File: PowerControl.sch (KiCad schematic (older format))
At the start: 22 parts, among them J1 Conn_01x02, J2 Emergency_stop_switch, J3 Emergency_stop_switch, J4 XT60PB-F, J5 XT60PB-M, Q1 Q_PMOS_GDS, Q2 Q_PMOS_GDS, U1 TLP621, U2 TLV76012DBZR

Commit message: Add board
基本的な設計が終了
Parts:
- added H1, H2, H3, H4: MountingHole, MountingHole:MountingHole_3.2mm_M3, symbol Mechanical:MountingHole
- C1: footprint (none) -> Capacitor_THT:CP_Radial_D12.5mm_P5.00mm
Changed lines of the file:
@@
 Wire Wire Line
 	8050 3900 8050 3950
-$Comp
-L power:VCC #PWR09
-U 1 1 5EF2872A
-P 6400 4950
-F 0 "#PWR09" H 6400 4800 50  0001 C CNN
-F 1 "VCC" H 6415 5123 50  0000 C CNN
-F 2 "" H 6400 4950 50  0001 C CNN
-F 3 "" H 6400 4950 50  0001 C CNN
-	1    6400 4950
-	1    0    0    -1
-$EndComp
 Text GLabel 8150 3800 0    50   Input ~ 0
 OutPut
@@
 Wire Wire Line
 	6400 5050 6400 5200
-Wire Wire Line
-	6400 4950 6400 5050
 Connection ~ 6400 5050
 $Comp
@@
 F 0 "C1" H 1868 3496 50  0000 L CNN
 F 1 "1000u" H 1868 3405 50  0000 L CNN
-F 2 "" H 1788 3300 50  0001 C CNN
+F 2 "Capacitor_THT:CP_Radial_D12.5mm_P5.00mm" H 1788 3300 50  0001 C CNN
 F 3 "~" H 1750 3450 50  0001 C CNN
 	1    1750 3450
@@
 Wire Wire Line
 	5250 5400 5700 5400
+Wire Wire Line
+	6400 4950 6400 5050
+$Comp
+L power:VCC #PWR09
+U 1 1 5EF2872A
+P 6400 4950
+F 0 "#PWR09" H 6400 4800 50  0001 C CNN
+F 1 "VCC" H 6415 5123 50  0000 C CNN
+F 2 "" H 6400 4950 50  0001 C CNN
+F 3 "" H 6400 4950 50  0001 C CNN
+	1    6400 4950
+	1    0    0    -1
+$EndComp
+$Comp
+L Mechanical:MountingHole H1
+U 1 1 5EF2F027
+P 5550 3450
+F 0 "H1" H 5650 3496 50  0000 L CNN
+F 1 "MountingHole" H 5650 3405 50  0000 L CNN
+F 2 "MountingHole:MountingHole_3.2mm_M3" H 5550 3450 50  0001 C CNN
+F 3 "~" H 5550 3450 50  0001 C CNN
+	1    5550 3450
+	1    0    0    -1
+$EndComp
+$Comp
+L Mechanical:MountingHole H3
+U 1 1 5EF2FEEF
+P 6250 3450
+F 0 "H3" H 6350 3496 50  0000 L CNN
+F 1 "MountingHole" H 6350 3405 50  0000 L CNN
+F 2 "MountingHole:MountingHole_3.2mm_M3" H 6250 3450 50  0001 C CNN
+F 3 "~" H 6250 3450 50  0001 C CNN
+	1    6250 3450
+	1    0    0    -1
+$EndComp
+$Comp
+L Mechanical:MountingHole H2
+U 1 1 5EF30E40
+P 5550 3650
+F 0 "H2" H 5650 3696 50  0000 L CNN
+F 1 "MountingHole" H 5650 3605 50  0000 L CNN
+F 2 "MountingHole:MountingHole_3.2mm_M3" H 5550 3650 50  0001 C CNN
+F 3 "~" H 5550 3650 50  0001 C CNN
+	1    5550 3650
+	1    0    0    -1
+$EndComp
+$Comp
+L Mechanical:MountingHole H4
+U 1 1 5EF31C67
+P 6250 3650
+F 0 "H4" H 6350 3696 50  0000 L CNN
+F 1 "MountingHole" H 6350 3605 50  0000 L CNN
+F 2 "MountingHole:MountingHole_3.2mm_M3" H 6250 3650 50  0001 C CNN
+F 3 "~" H 6250 3650 50  0001 C CNN
+	1    6250 3650
+	1    0    0    -1
+$EndComp
 $EndSCHEMATC

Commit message: change Pch MOSFET name
Pch MOSFETの名称をIPD80P03P4L-07に変更
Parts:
- Q1, Q2: value Q_PMOS_GDS -> IPD80P03P4L-07
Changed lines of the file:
@@
 U 1 1 5EF097AB
 P 6300 5400
-F 0 "Q1" H 6505 5354 50  0000 L CNN
-F 1 "Q_PMOS_GDS" H 6505 5445 50  0000 L CNN
+F 0 "Q1" H 6504 5354 50  0000 L CNN
+F 1 "IPD80P03P4L-07" H 6504 5445 50  0000 L CNN
 F 2 "Package_TO_SOT_SMD:TO-252-2" H 6500 5500 50  0001 C CNN
 F 3 "~" H 6300 5400 50  0001 C CNN
@@
 U 1 1 5EF2BF51
 P 7300 5400
-F 0 "Q2" H 7505 5354 50  0000 L CNN
-F 1 "Q_PMOS_GDS" H 7505 5445 50  0000 L CNN
+F 0 "Q2" H 7504 5354 50  0000 L CNN
+F 1 "IPD80P03P4L-07" H 7504 5445 50  0000 L CNN
 F 2 "Package_TO_SOT_SMD:TO-252-2" H 7500 5500 50  0001 C CNN
 F 3 "~" H 7300 5400 50  0001 C CNN

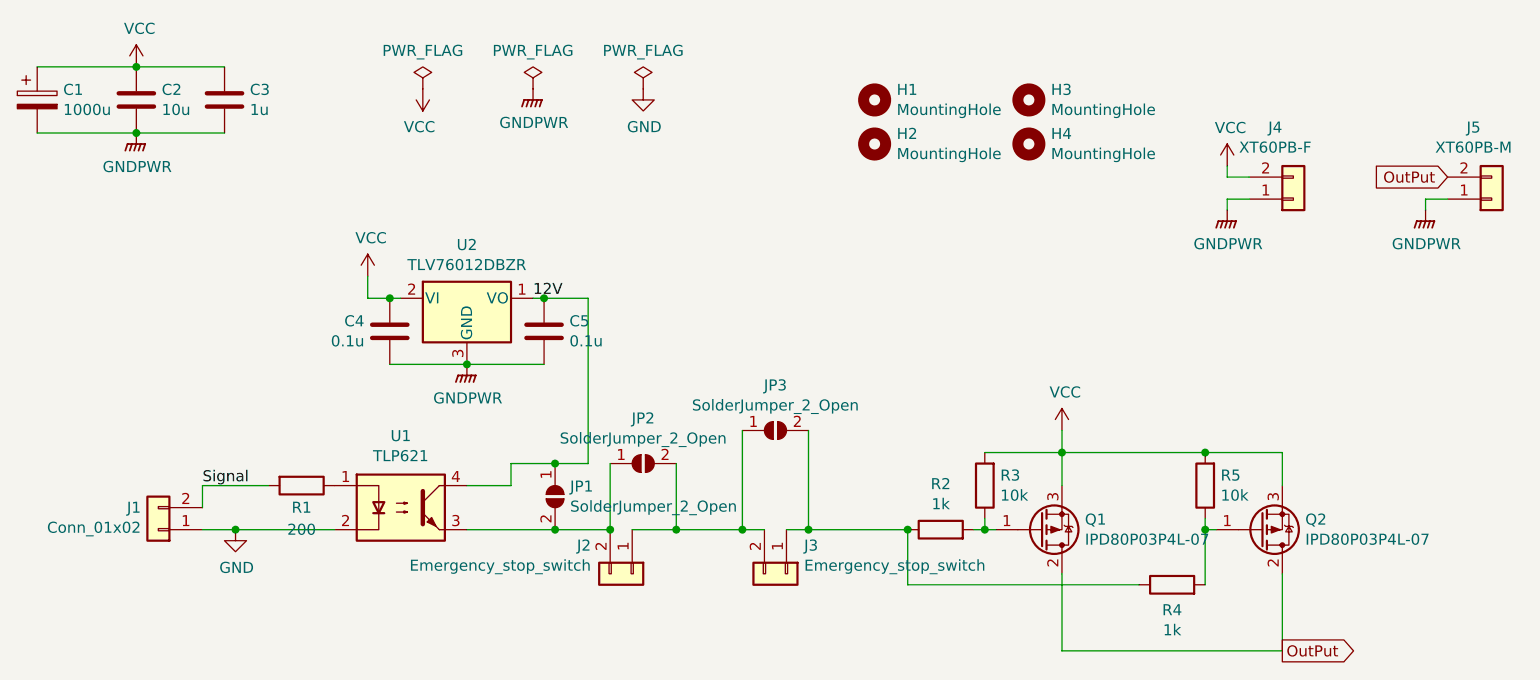
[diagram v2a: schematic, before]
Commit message: Fix: Pch MOSFETのゲートの印加電圧を修正(12V→GND)
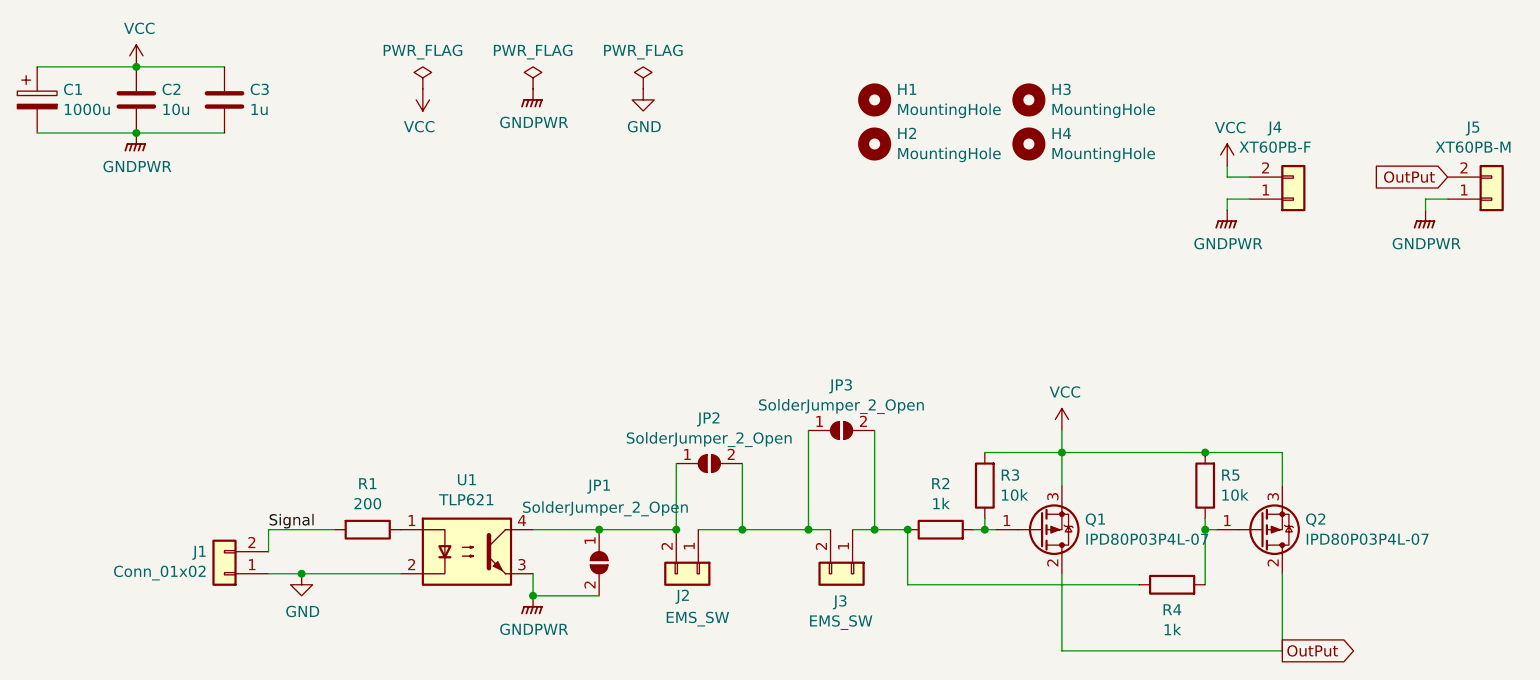
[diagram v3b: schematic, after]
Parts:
- removed C4, C5: 0.1u, Capacitor_SMD:C_0805_2012Metric_Pad1.15x1.40mm_HandSolder, symbol Device:C
- removed U2: TLV76012DBZR, Package_TO_SOT_SMD:TSOT-23_HandSoldering, symbol Regulator_Linear:LM3480-12
- J2, J3: value Emergency_stop_switch -> EMS_SW
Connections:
- net 12V is gone; now on an unnamed net: JP1.1 (A), U1.4
- net GNDPWR: now also JP1.2 (B), U1.3
- net at J2.2 (Pin_2), JP2.1 (A): no longer JP1.2 (B), U1.3
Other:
- moved on the sheet: J1, J2, J3, JP1, JP2, JP3, R1, U1
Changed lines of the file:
@@
-	1    0    0    -1
-$EndComp
-Text Label 2500 5200 0    50   ~ 0
-Signal
-Wire Wire Line
-	2500 5300 2500 5200
-Wire Wire Line
-	2650 5400 2500 5400
-$Comp
-L power:GND #PWR03
-U 1 1 5EF1071A
-P 2650 5400
-F 0 "#PWR03" H 2650 5150 50  0001 C CNN
-F 1 "GND" H 2655 5227 50  0000 C CNN
-F 2 "" H 2650 5400 50  0001 C CNN
-F 3 "" H 2650 5400 50  0001 C CNN
-	1    2650 5400
-	1    0    0    -1
-$EndComp
-$Comp
-L Connector_Generic:Conn_01x02 J1
-U 1 1 5EF109E6
-P 2300 5400
-F 0 "J1" H 2379 5300 50  0000 L CNN
-F 1 "Conn_01x02" H 2379 5391 50  0000 L CNN
-F 2 "Connector_PinHeader_2.54mm:PinHeader_1x02_P2.54mm_Vertical" H 2300 5400 50  0001 C CNN
-F 3 "~" H 2300 5400 50  0001 C CNN
-	1    2300 5400
-	-1   0    0    1
-$EndComp
-$Comp
-L Isolator:PC817 U1
-U 1 1 5EF0F04E
-P 3400 5300
-F 0 "U1" H 3400 5625 50  0000 C CNN
-F 1 "TLP621" H 3400 5534 50  0000 C CNN
-F 2 "Package_DIP:DIP-4_W7.62mm" H 3200 5100 50  0001 L CIN
-F 3 "http://www.soselectronic.cz/a_info/resource/d/pc817.pdf" H 3400 5300 50  0001 L CNN
-	1    3400 5300
 	1    0    0    -1
 $EndComp
@@
 Connection ~ 6400 5050
 $Comp
-L Device:R R1
-U 1 1 5EF32C60
-P 2950 5200
-F 0 "R1" V 3050 5200 50  0000 C CNN
-F 1 "200" V 3150 5200 50  0000 C CNN
-F 2 "Resistor_SMD:R_0603_1608Metric_Pad1.05x0.95mm_HandSolder" V 2880 5200 50  0001 C CNN
-F 3 "~" H 2950 5200 50  0001 C CNN
-	1    2950 5200
-	0    1    1    0
-$EndComp
-Connection ~ 2650 5400
-Wire Wire Line
-	2650 5400 3100 5400
-Wire Wire Line
-	2500 5200 2800 5200
-$Comp
-L Connector_Generic:Conn_01x02 J2
-U 1 1 5EF40D5E
-P 4450 5600
-F 0 "J2" V 4322 5413 50  0000 R CNN
-F 1 "Emergency_stop_switch" V 4413 5413 50  0000 R CNN
-F 2 "Connector_PinHeader_2.54mm:PinHeader_1x02_P2.54mm_Vertical" H 4450 5600 50  0001 C CNN
-F 3 "~" H 4450 5600 50  0001 C CNN
-	1    4450 5600
-	0    1    1    0
-$EndComp
-$Comp
-L Connector_Generic:Conn_01x02 J3
-U 1 1 5EF41305
-P 5150 5600
-F 0 "J3" V 5022 5680 50  0000 L CNN
-F 1 "Emergency_stop_switch" V 5113 5680 50  0000 L CNN
-F 2 "Connector_PinHeader_2.54mm:PinHeader_1x02_P2.54mm_Vertical" H 5150 5600 50  0001 C CNN
-F 3 "~" H 5150 5600 50  0001 C CNN
-	1    5150 5600
-	0    1    1    0
-$EndComp
-Wire Wire Line
-	3250 4250 3250 4350
-$Comp
-L power:VCC #PWR04
-U 1 1 5EF16864
-P 3250 4250
-F 0 "#PWR04" H 3250 4100 50  0001 C CNN
-F 1 "VCC" H 3265 4423 50  0000 C CNN
-F 2 "" H 3250 4250 50  0001 C CNN
-F 3 "" H 3250 4250 50  0001 C CNN
-	1    3250 4250
-	1    0    0    -1
-$EndComp
-$Comp
-L Regulator_Linear:LM3480-12 U2
-U 1 1 5EF1540F
-P 3700 4350
-F 0 "U2" H 3700 4592 50  0000 C CNN
-F 1 "TLV76012DBZR" H 3700 4501 50  0000 C CNN
-F 2 "Package_TO_SOT_SMD:TSOT-23_HandSoldering" H 3725 4200 50  0001 L CIN
-F 3 "" H 3700 4300 50  0001 C CNN
-	1    3700 4350
-	1    0    0    -1
-$EndComp
-Wire Wire Line
-	4250 4350 4250 5100
-$Comp
 L Connector_Generic:Conn_01x02 J4
 U 1 1 5EF2467C
@@
 	1    0    0    1
 $EndComp
-Wire Wire Line
-	4000 4350 4050 4350
-$Comp
-L power:GNDPWR #PWR06
-U 1 1 5EF1CE2F
-P 3700 4650
-F 0 "#PWR06" H 3700 4450 50  0001 C CNN
-F 1 "GNDPWR" H 3704 4496 50  0000 C CNN
-F 2 "" H 3700 4600 50  0001 C CNN
-F 3 "" H 3700 4600 50  0001 C CNN
-	1    3700 4650
-	1    0    0    -1
-$EndComp
-Text Label 4000 4350 0    50   ~ 0
-12V
 $Comp
 L Device:Q_PMOS_GDS Q2
@@
 $EndComp
 $Comp
-L Device:C C5
-U 1 1 5EF510BF
-P 4050 4500
-F 0 "C5" H 4165 4546 50  0000 L CNN
-F 1 "0.1u" H 4165 4455 50  0000 L CNN
-F 2 "Capacitor_SMD:C_0805_2012Metric_Pad1.15x1.40mm_HandSolder" H 4088 4350 50  0001 C CNN
-F 3 "~" H 4050 4500 50  0001 C CNN
-	1    4050 4500
-	1    0    0    -1
-$EndComp
-$Comp
-L Device:C C4
-U 1 1 5EF519D9
-P 3350 4500
-F 0 "C4" H 3235 4546 50  0000 R CNN
-F 1 "0.1u" H 3235 4455 50  0000 R CNN
-F 2 "Capacitor_SMD:C_0805_2012Metric_Pad1.15x1.40mm_HandSolder" H 3388 4350 50  0001 C CNN
-F 3 "~" H 3350 4500 50  0001 C CNN
-	1    3350 4500
-	1    0    0    -1
-$EndComp
-Connection ~ 4050 4350
-Wire Wire Line
-	3700 5200 3900 5200
-Wire Wire Line
-	3250 4350 3350 4350
-Connection ~ 3350 4350
-Wire Wire Line
-	3350 4350 3400 4350
-Wire Wire Line
-	4050 4650 3700 4650
-Connection ~ 3700 4650
-Wire Wire Line
-	3700 4650 3350 4650
-Wire Wire Line
-	4050 4350 4250 4350
-$Comp
 L Device:CP C1
 U 1 1 5EF5DFD2
@@
 $EndComp
 Wire Wire Line
-	3900 5100 3900 5200
-Connection ~ 4100 5100
-Wire Wire Line
-	4100 5100 3900 5100
-Wire Wire Line
-	4100 5100 4250 5100
-Wire Wire Line
-	3700 5400 4100 5400
-Connection ~ 4100 5400
-Wire Wire Line
-	4100 5400 4350 5400
-$Comp
-L Jumper:SolderJumper_2_Open JP3
-U 1 1 5EF13331
-P 5100 4950
-F 0 "JP3" H 5100 5155 50  0000 C CNN
-F 1 "SolderJumper_2_Open" H 5100 5064 50  0000 C CNN
-F 2 "Jumper:SolderJumper-2_P1.3mm_Open_TrianglePad1.0x1.5mm" H 5100 4950 50  0001 C CNN
-F 3 "~" H 5100 4950 50  0001 C CNN
-	1    5100 4950
-	1    0    0    -1
-$EndComp
-$Comp
-L Jumper:SolderJumper_2_Open JP2
-U 1 1 5EF3F971
-P 4500 5100
-F 0 "JP2" H 4500 5305 50  0000 C CNN
-F 1 "SolderJumper_2_Open" H 4500 5214 50  0000 C CNN
-F 2 "Jumper:SolderJumper-2_P1.3mm_Open_TrianglePad1.0x1.5mm" H 4500 5100 50  0001 C CNN
-F 3 "~" H 4500 5100 50  0001 C CNN
-	1    4500 5100
-	1    0    0    -1
-$EndComp
-$Comp
-L Jumper:SolderJumper_2_Open JP1
-U 1 1 5EF1E5F2
-P 4100 5250
-F 0 "JP1" V 4054 5318 50  0000 L CNN
-F 1 "SolderJumper_2_Open" V 4145 5318 50  0000 L CNN
-F 2 "Jumper:SolderJumper-2_P1.3mm_Open_TrianglePad1.0x1.5mm" H 4100 5250 50  0001 C CNN
-F 3 "~" H 4100 5250 50  0001 C CNN
-	1    4100 5250
-	0    1    1    0
-$EndComp
-Wire Wire Line
-	5150 5400 5250 5400
-Wire Wire Line
-	4450 5400 4650 5400
-Wire Wire Line
-	4350 5100 4350 5400
-Connection ~ 4350 5400
-Wire Wire Line
-	4650 5100 4650 5400
-Connection ~ 4650 5400
-Wire Wire Line
-	4650 5400 4950 5400
-Wire Wire Line
-	4950 4950 4950 5400
-Connection ~ 4950 5400
-Wire Wire Line
-	4950 5400 5050 5400
+	5450 5400 5550 5400
 Wire Wire Line
 	5250 4950 5250 5400
 Connection ~ 5250 5400
 Wire Wire Line
-	5250 5400 5700 5400
+	5250 5400 5350 5400
+Wire Wire Line
+	5550 4950 5550 5400
+Connection ~ 5550 5400
+Wire Wire Line
+	5550 5400 5700 5400
 Wire Wire Line
 	6400 4950 6400 5050
@@
 	1    0    0    -1
 $EndComp
+$Comp
+L Connector_Generic:Conn_01x02 J3
+U 1 1 5EF41305
+P 5450 5600
+F 0 "J3" V 5575 5546 50  0000 C CNN
+F 1 "EMS_SW" V 5666 5546 50  0000 C CNN
+F 2 "Connector_PinHeader_2.54mm:PinHeader_1x02_P2.54mm_Vertical" H 5450 5600 50  0001 C CNN
+F 3 "~" H 5450 5600 50  0001 C CNN
+	1    5450 5600
+	0    1    1    0
+$EndComp
+Text Label 2800 5400 0    50   ~ 0
+Signal
+Wire Wire Line
+	2800 5500 2800 5400
+Wire Wire Line
+	2950 5600 2800 5600
+$Comp
+L power:GND #PWR03
+U 1 1 5EF1071A
+P 2950 5600
+F 0 "#PWR03" H 2950 5350 50  0001 C CNN
+F 1 "GND" H 2955 5427 50  0000 C CNN
+F 2 "" H 2950 5600 50  0001 C CNN
+F 3 "" H 2950 5600 50  0001 C CNN
+	1    2950 5600
+	1    0    0    -1
+$EndComp
+$Comp
+L Connector_Generic:Conn_01x02 J1
+U 1 1 5EF109E6
+P 2600 5600
+F 0 "J1" H 2679 5500 50  0000 L CNN
+F 1 "Conn_01x02" H 2679 5591 50  0000 L CNN
+F 2 "Connector_PinHeader_2.54mm:PinHeader_1x02_P2.54mm_Vertical" H 2600 5600 50  0001 C CNN
+F 3 "~" H 2600 5600 50  0001 C CNN
+	1    2600 5600
+	-1   0    0    1
+$EndComp
+$Comp
+L Device:R R1
+U 1 1 5EF32C60
+P 3250 5400
+F 0 "R1" V 3043 5400 50  0000 C CNN
+F 1 "200" V 3134 5400 50  0000 C CNN
+F 2 "Resistor_SMD:R_0603_1608Metric_Pad1.05x0.95mm_HandSolder" V 3180 5400 50  0001 C CNN
+F 3 "~" H 3250 5400 50  0001 C CNN
+	1    3250 5400
+	0    1    1    0
+$EndComp
+Connection ~ 2950 5600
+Wire Wire Line
+	2950 5600 3400 5600
+Wire Wire Line
+	2800 5400 3100 5400
+$Comp
+L Connector_Generic:Conn_01x02 J2
+U 1 1 5EF40D5E
+P 4750 5600
+F 0 "J2" V 4850 5500 50  0000 L CNN
+F 1 "EMS_SW" V 4950 5450 50  0000 L CNN
+F 2 "Connector_PinHeader_2.54mm:PinHeader_1x02_P2.54mm_Vertical" H 4750 5600 50  0001 C CNN
+F 3 "~" H 4750 5600 50  0001 C CNN
+	1    4750 5600
+	0    1    1    0
+$EndComp
+$Comp
+L Jumper:SolderJumper_2_Open JP1
+U 1 1 5EF1E5F2
+P 4300 5550
+F 0 "JP1" V 3950 5500 50  0000 L CNN
+F 1 "SolderJumper_2_Open" V 4050 5200 50  0000 L CNN
+F 2 "Jumper:SolderJumper-2_P1.3mm_Open_TrianglePad1.0x1.5mm" H 4300 5550 50  0001 C CNN
+F 3 "~" H 4300 5550 50  0001 C CNN
+	1    4300 5550
+	0    1    1    0
+$EndComp
+Wire Wire Line
+	4750 5400 4950 5400
+Wire Wire Line
+	4650 5100 4650 5400
+Connection ~ 4650 5400
+$Comp
+L Isolator:PC817 U1
+U 1 1 5EF0F04E
+P 3700 5500
+F 0 "U1" H 3700 5825 50  0000 C CNN
+F 1 "TLP621" H 3700 5734 50  0000 C CNN
+F 2 "Package_DIP:DIP-4_W7.62mm" H 3500 5300 50  0001 L CIN
+F 3 "http://www.soselectronic.cz/a_info/resource/d/pc817.pdf" H 3700 5500 50  0001 L CNN
+	1    3700 5500
+	1    0    0    -1
+$EndComp
+Wire Wire Line
+	4000 5400 4300 5400
+$Comp
+L power:GNDPWR #PWR?
+U 1 1 61447DCE
+P 4000 5700
+F 0 "#PWR?" H 4000 5500 50  0001 C CNN
+F 1 "GNDPWR" H 4004 5546 50  0000 C CNN
+F 2 "" H 4000 5650 50  0001 C CNN
+F 3 "" H 4000 5650 50  0001 C CNN
+	1    4000 5700
+	1    0    0    -1
+$EndComp
+Connection ~ 4300 5400
+Wire Wire Line
+	4300 5400 4650 5400
+Wire Wire Line
+	4000 5600 4000 5700
+Wire Wire Line
+	4000 5700 4300 5700
+Connection ~ 4000 5700
+Wire Wire Line
+	4950 5400 5250 5400
+Connection ~ 4950 5400
+Wire Wire Line
+	4950 5100 4950 5400
+$Comp
+L Jumper:SolderJumper_2_Open JP3
+U 1 1 5EF13331
+P 5400 4950
+F 0 "JP3" H 5400 5155 50  0000 C CNN
+F 1 "SolderJumper_2_Open" H 5400 5064 50  0000 C CNN
+F 2 "Jumper:SolderJumper-2_P1.3mm_Open_TrianglePad1.0x1.5mm" H 5400 4950 50  0001 C CNN
+F 3 "~" H 5400 4950 50  0001 C CNN
+	1    5400 4950
+	1    0    0    -1
+$EndComp
+$Comp
+L Jumper:SolderJumper_2_Open JP2
+U 1 1 5EF3F971
+P 4800 5100
+F 0 "JP2" H 4800 5305 50  0000 C CNN
+F 1 "SolderJumper_2_Open" H 4800 5214 50  0000 C CNN
+F 2 "Jumper:SolderJumper-2_P1.3mm_Open_TrianglePad1.0x1.5mm" H 4800 5100 50  0001 C CNN
+F 3 "~" H 4800 5100 50  0001 C CNN
+	1    4800 5100
+	1    0    0    -1
+$EndComp
